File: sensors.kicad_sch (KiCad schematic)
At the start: 12 parts, among them U2 SAM-M10Q-00B, U3 LSM6DSOX, U4 LIS2MDL, U5 LPS22DF

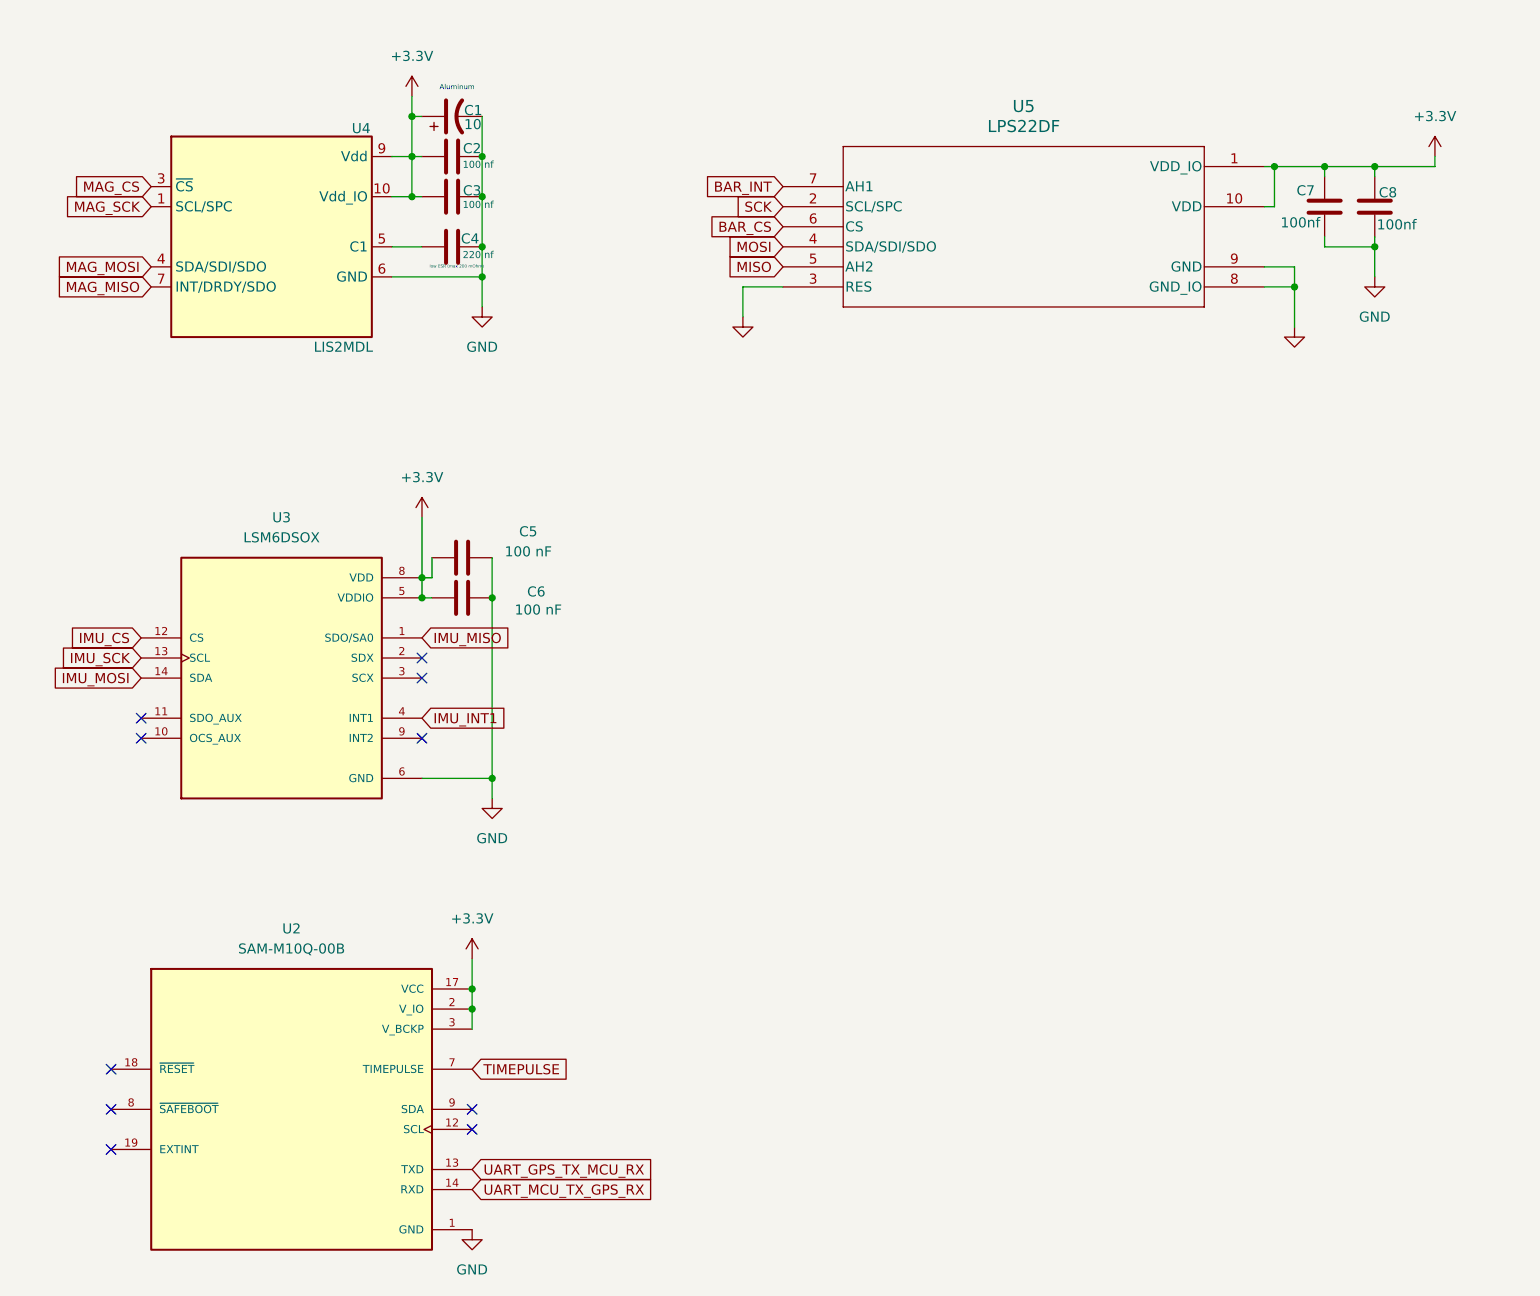
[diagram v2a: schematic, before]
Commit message: Fixed the second round of issues Sam gave us
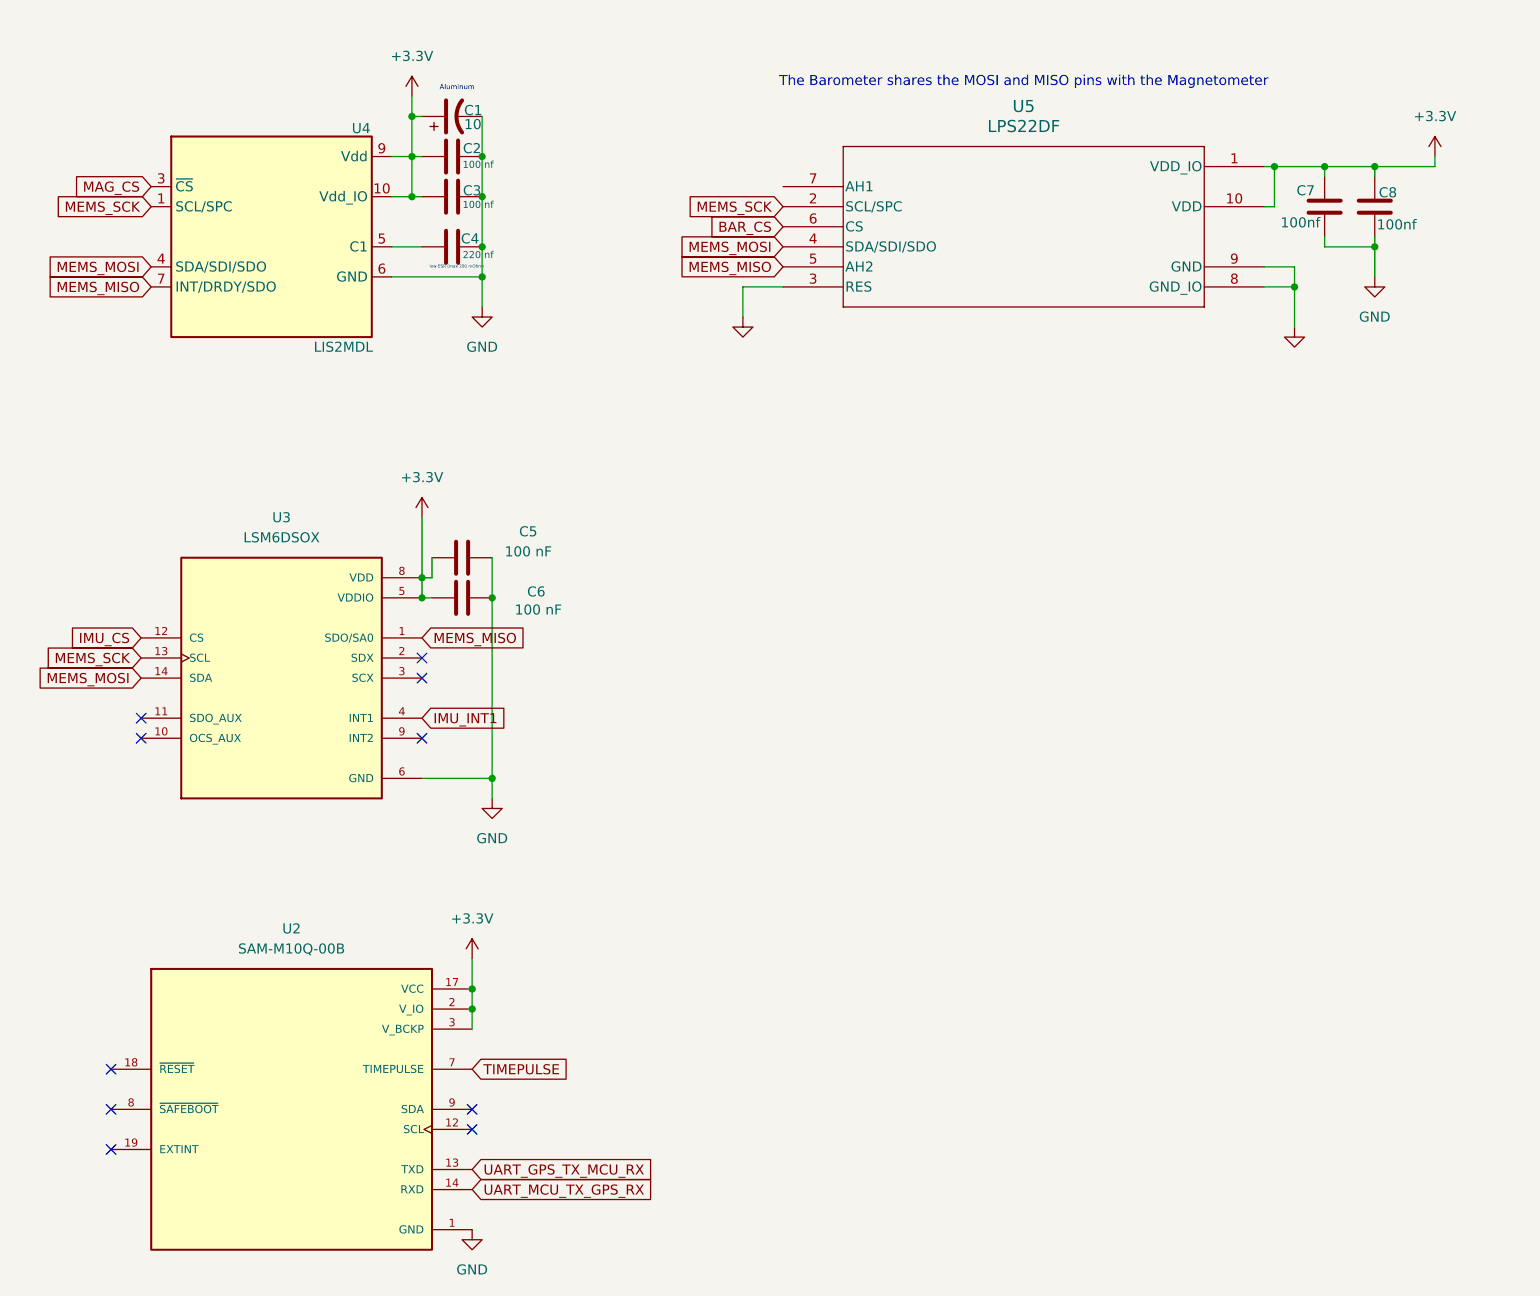
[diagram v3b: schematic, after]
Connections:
- net MAG_MISO is gone; now on net MEMS_MISO: U4.7 (INT/DRDY/SDO)
- net MAG_MOSI is gone; now on net MEMS_MOSI: U4.4 (SDA/SDI/SDO)
- net MAG_SCK is gone; now on net MEMS_SCK: U4.1 (SCL/SPC)
- net MISO is gone; now on net MEMS_MISO: U5.5 (AH2)
- net MOSI is gone; now on net MEMS_MOSI: U5.4 (SDA/SDI/SDO)
- net SCK is gone; now on net MEMS_SCK: U5.2 (SCL/SPC)
- net BAR_INT: no longer names the net of U5.7 (AH1)
- net IMU_MISO renamed MEMS_MISO
- net IMU_MOSI renamed MEMS_MOSI
- net IMU_SCK renamed MEMS_SCK
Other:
- note added: "The Barometer shares the MOSI and MISO pins with the Magnetometer"
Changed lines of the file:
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@@
 	(generator_version "9.0")
 	(paper "A4")
+	(text "The Barometer shares the MOSI and MISO pins with the Magnetometer"
+		(exclude_from_sim no)
+		(at 160.02 29.972 0)
+		(effects
+			(font
+				(size 1.27 1.27)
+			)
+		)
+	)
 	(text_box "Aluminum"
 		(exclude_from_sim no)
@@
 		)
 	)
-	(global_label "MAG_MOSI"
+	(global_label "MEMS_MOSI"
 		(shape input)
 		(at 49.53 53.34 180)
@@
 		)
 		(property "Intersheetrefs" "${INTERSHEET_REFS}"
-			(at 37.171 53.34 0)
+			(at 35.7197 53.34 0)
 			(effects
 				(font
@@
 		)
 	)
-	(global_label "IMU_MOSI"
+	(global_label "MEMS_MOSI"
 		(shape input)
 		(at 48.26 105.41 180)
@@
 		)
 		(property "Intersheetrefs" "${INTERSHEET_REFS}"
-			(at 36.3243 105.41 0)
+			(at 34.4497 105.41 0)
 			(effects
 				(font
@@
 		)
 	)
-	(global_label "MAG_MISO"
+	(global_label "MEMS_MISO"
 		(shape input)
 		(at 49.53 55.88 180)
@@
 		)
 		(property "Intersheetrefs" "${INTERSHEET_REFS}"
-			(at 37.171 55.88 0)
+			(at 35.7197 55.88 0)
 			(effects
 				(font
@@
 		)
 	)
-	(global_label "MISO"
+	(global_label "MEMS_MISO"
 		(shape input)
 		(at 129.54 53.34 180)
@@
 		)
 		(property "Intersheetrefs" "${INTERSHEET_REFS}"
-			(at 121.9586 53.34 0)
+			(at 115.7297 53.34 0)
 			(effects
 				(font
@@
 		)
 	)
-	(global_label "BAR_INT"
-		(shape input)
-		(at 129.54 43.18 180)
+	(global_label "MEMS_MOSI"
+		(shape input)
+		(at 129.54 50.8 180)
 		(fields_autoplaced yes)
 		(effects
@@
 		)
 		(property "Intersheetrefs" "${INTERSHEET_REFS}"
-			(at 119.0557 43.18 0)
+			(at 115.7297 50.8 0)
 			(effects
 				(font
@@
 		)
 	)
-	(global_label "MOSI"
-		(shape input)
-		(at 129.54 50.8 180)
+	(global_label "MEMS_SCK"
+		(shape input)
+		(at 129.54 45.72 180)
 		(fields_autoplaced yes)
 		(effects
@@
 		)
 		(property "Intersheetrefs" "${INTERSHEET_REFS}"
-			(at 121.9586 50.8 0)
+			(at 116.5764 45.72 0)
 			(effects
 				(font
@@
 		)
 	)
-	(global_label "SCK"
-		(shape input)
-		(at 129.54 45.72 180)
+	(global_label "MEMS_SCK"
+		(shape input)
+		(at 49.53 45.72 180)
 		(fields_autoplaced yes)
 		(effects
@@
 		)
 		(property "Intersheetrefs" "${INTERSHEET_REFS}"
-			(at 122.8053 45.72 0)
+			(at 36.5664 45.72 0)
 			(effects
 				(font
@@
 		)
 	)
-	(global_label "MAG_SCK"
-		(shape input)
-		(at 49.53 45.72 180)
+	(global_label "TIMEPULSE"
+		(shape input)
+		(at 90.17 154.94 0)
+		(fields_autoplaced yes)
+		(effects
+			(font
+				(size 1.27 1.27)
+			)
+			(justify left)
+		)
+		(property "Intersheetrefs" "${INTERSHEET_REFS}"
+			(at 103.3151 154.94 0)
+			(effects
+				(font
+					(size 1.27 1.27)
+				)
+				(justify left)
+				(hide yes)
+			)
+		)
+	)
+	(global_label "MEMS_MISO"
+		(shape input)
+		(at 83.82 100.33 0)
+		(fields_autoplaced yes)
+		(effects
+			(font
+				(size 1.27 1.27)
+			)
+			(justify left)
+		)
+		(property "Intersheetrefs" "${INTERSHEET_REFS}"
+			(at 97.6303 100.33 0)
+			(effects
+				(font
+					(size 1.27 1.27)
+				)
+				(justify left)
+				(hide yes)
+			)
+		)
+	)
+	(global_label "BAR_CS"
+		(shape input)
+		(at 129.54 48.26 180)
 		(fields_autoplaced yes)
 		(effects
@@
 		)
 		(property "Intersheetrefs" "${INTERSHEET_REFS}"
-			(at 38.0177 45.72 0)
+			(at 119.4791 48.26 0)
 			(effects
 				(font
@@
 		)
 	)
-	(global_label "TIMEPULSE"
-		(shape input)
-		(at 90.17 154.94 0)
-		(fields_autoplaced yes)
-		(effects
-			(font
-				(size 1.27 1.27)
-			)
-			(justify left)
-		)
-		(property "Intersheetrefs" "${INTERSHEET_REFS}"
-			(at 103.3151 154.94 0)
-			(effects
-				(font
-					(size 1.27 1.27)
-				)
-				(justify left)
-				(hide yes)
-			)
-		)
-	)
-	(global_label "IMU_MISO"
-		(shape input)
-		(at 83.82 100.33 0)
-		(fields_autoplaced yes)
-		(effects
-			(font
-				(size 1.27 1.27)
-			)
-			(justify left)
-		)
-		(property "Intersheetrefs" "${INTERSHEET_REFS}"
-			(at 95.7557 100.33 0)
-			(effects
-				(font
-					(size 1.27 1.27)
-				)
-				(justify left)
-				(hide yes)
-			)
-		)
-	)
-	(global_label "BAR_CS"
-		(shape input)
-		(at 129.54 48.26 180)
+	(global_label "MEMS_SCK"
+		(shape input)
+		(at 48.26 102.87 180)
 		(fields_autoplaced yes)
 		(effects
@@
 		)
 		(property "Intersheetrefs" "${INTERSHEET_REFS}"
-			(at 119.4791 48.26 0)
-			(effects
-				(font
-					(size 1.27 1.27)
-				)
-				(justify right)
-				(hide yes)
-			)
-		)
-	)
-	(global_label "IMU_SCK"
-		(shape input)
-		(at 48.26 102.87 180)
-		(fields_autoplaced yes)
-		(effects
-			(font
-				(size 1.27 1.27)
-			)
-			(justify right)
-		)
-		(property "Intersheetrefs" "${INTERSHEET_REFS}"
-			(at 37.171 102.87 0)
-			(effects
-				(font
+			(at 35.2964 102.87 0)
+			(effects
+				(font

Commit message: Finished the footprint for the Micro Controller
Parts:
- C7, C8: footprint (none) -> Capacitor_SMD:C_0603_1608Metric

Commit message: Just a few quick edits but only small
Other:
- note removed: "The Barometer shares the MOSI and MISO pins with the Magnetometer"
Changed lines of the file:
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@@
 	(generator_version "10.0")
 	(paper "A4")
-	(text "The Barometer shares the MOSI and MISO pins with the Magnetometer"
-		(exclude_from_sim no)
-		(at 160.02 29.972 0)
-		(effects
-			(font
-				(size 1.27 1.27)
-			)
-		)
-	)
 	(text_box "Aluminum"
 		(exclude_from_sim no)
